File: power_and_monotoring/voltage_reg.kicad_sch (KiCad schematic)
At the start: 15 parts, among them IC1 ADP3335ARMZ-5-R7, IC2 ADP3335ARMZ-3.3-RL, J1 Microfit_01x02_Vertical, U10 P783-Q24-S3-S

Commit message: before design review
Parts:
- removed GLV_MASTER_IN1: GREEN, LTST-S270KGKT, UniSA_Motorsport_Diode:0605, symbol UniSA_Motorsport_Diode:LTST-S270KGKT
- added D5: GREEN, UniSA_Motorsport_Diode:0805, symbol UniSA_Motorsport_Diode:LED_0805
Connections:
- net GND: now also D5.1 (K)
- net at R39.2: now also D5.2 (A)
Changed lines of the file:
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@@
     (stroke (width 0) (type default))
   )
-  (wire (pts (xy 135.89 147.32) (xy 135.89 156.21))
+  (wire (pts (xy 135.89 139.7) (xy 135.89 156.21))
     (stroke (width 0) (type default))
   )
@@
         (path "/e288a49a-7ef7-4ddb-8751-b5872bff5868/00000000-0000-0000-0000-00005fc1883e"
           (reference "#PWR026") (unit 1)
+        )
+      )
+    )
+  )
+  (symbol (lib_id "UniSA_Motorsport_Diode:LED_0805") (at 135.89 135.89 90) (unit 1)
+    (in_bom yes) (on_board yes) (dnp no) (fields_autoplaced)
+    (property "Reference" "D5" (at 139.065 136.8552 90)
+      (effects (font (size 1.27 1.27)) (justify right))
+    )
+    (property "Value" "GREEN" (at 139.065 139.3952 90)
+      (effects (font (size 1.27 1.27)) (justify right))
+    )
+    (property "Footprint" "UniSA_Motorsport_Diode:0805" (at 135.89 135.89 0)
+      (effects (font (size 1.27 1.27)) hide)
+    )
+    (property "Datasheet" "https://au.mouser.com/datasheet/2/109/Dialight_CBI_data_599-0805_Apr2018-1370606.pdf" (at 135.89 135.89 0)
+      (effects (font (size 1.27 1.27)) hide)
+    )
+    (property "Color" "Red, Blue, Green, Orange, Yellow" (at 130.81 135.89 0)
+      (effects (font (size 1.27 1.27)) hide)
+    )
+    (pin "1")
+    (pin "2")
+    (instances
+      (project "power_and_monotoring"
+        (path "/09bdaed7-9abd-4a06-aca9-25dcfc39eec3/22f29577-e4ea-44ad-b176-4b72d277bfff"
+          (reference "D5") (unit 1)
+        )
+        (path "/09bdaed7-9abd-4a06-aca9-25dcfc39eec3/07532015-f4dd-4bfc-83f6-71cf6465f622"
+          (reference "D9") (unit 1)
+        )
+        (path "/09bdaed7-9abd-4a06-aca9-25dcfc39eec3/7e02ab45-3a69-40b9-bad8-957e9bf8bfd2"
+          (reference "D11") (unit 1)
         )
       )
@@
         )
       )
-    )
-  )
-  (symbol (lib_id "UniSA_Motorsport_Diode:LTST-S270KGKT") (at 135.89 139.7 90) (unit 1)
-    (in_bom yes) (on_board yes) (dnp no)
-    (property "Reference" "GLV_MASTER_IN1" (at 131.445 146.685 0)
-      (effects (font (size 1.27 1.27)))
-    )
-    (property "Value" "GREEN, LTST-S270KGKT" (at 129.54 149.225 0)
-      (effects (font (size 1.27 1.27)))
-    )
-    (property "Footprint" "UniSA_Motorsport_Diode:0605" (at 140.64 151.13 0)
-      (effects (font (size 1.27 1.27)) (justify left bottom) hide)
-    )
-    (property "Datasheet" "https://optoelectronics.liteon.com/upload/download/DS22-2000-226/LTST-S270KGKT.pdf" (at 140.97 182.88 0)
-      (effects (font (size 1.27 1.27)) (justify left bottom) hide)
-    )
-    (property "Height" "0.7" (at 529.54 127 0)
-      (effects (font (size 1.27 1.27)) (justify left bottom) hide)
-    )
-    (property "Mouser Part Number" "859-LTST-S270KGKT" (at 629.54 127 0)
-      (effects (font (size 1.27 1.27)) (justify left bottom) hide)
-    )
-    (property "Mouser Price/Stock" "https://www.mouser.co.uk/ProductDetail/Lite-On/LTST-S270KGKT?qs=oL5uk4n%2FG821%2FMiCU6RADg%3D%3D" (at 729.54 127 0)
-      (effects (font (size 1.27 1.27)) (justify left bottom) hide)
-    )
-    (property "Manufacturer_Name" "Lite-On" (at 829.54 127 0)
-      (effects (font (size 1.27 1.27)) (justify left bottom) hide)
-    )
-    (property "Manufacturer_Part_Number" "LTST-S270KGKT" (at 929.54 127 0)
-      (effects (font (size 1.27 1.27)) (justify left bottom) hide)
-    )
-    (pin "1")
-    (pin "2")
-    (instances
-      (project "power_and_monotoring"
-        (path "/09bdaed7-9abd-4a06-aca9-25dcfc39eec3/07532015-f4dd-4bfc-83f6-71cf6465f622"
-          (reference "GLV_MASTER_IN1") (unit 1)
-        )
-        (path "/09bdaed7-9abd-4a06-aca9-25dcfc39eec3/7e02ab45-3a69-40b9-bad8-957e9bf8bfd2"
-          (reference "LED11") (unit 1)
-        )
-      )

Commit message: Final
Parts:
- removed C16, C17: C, Capacitor_SMD:C_0805_2012Metric, symbol Device:C
- removed TP1: TestPoint, TestPoint:TestPoint_Pad_D2.0mm, symbol Connector:TestPoint
- removed U10: P783-Q24-S3-S, UniSA_Motorsport_Others:P783-Q24-S3-S, symbol UniSA_Motorsport_Regulator:P783-Q24-S3-S
- added 12V1: TestPoint, TestPoint:TestPoint_Pad_D2.0mm, symbol Connector:TestPoint
- added C6: 100uF, UniSA_Motorsport_Capacitor:EEEFK0J332AQ, symbol UniSA_Motorsport_Capacitor:EEE-FK1H101P
- added C8: EEV-FK1H391Q, UniSA_Motorsport_Capacitor:EEEFK0J332AQ, symbol UniSA_Motorsport_Capacitor:EEV-FK1H391Q
- added D27: NRVTS245ESFT1G, UniSA_Motorsport_Diode:SOD-123FL-2, symbol UniSA_Motorsport_Diode:NRVTS245ESFT1G
- added IC3: LM2576-12WU-TR, UniSA_Motorsport_SO:TO-263-5, symbol UniSA_Motorsport_Regulator:LM2576-12WU-TR
- added L1: 100uH, UniSA_Motorsport_Inductor:5050, symbol UniSA_Motorsport_Inductor:SRR1260-101M
- R23: renamed from R39; Resistance 68K -> 1K
- renumbered TP1 to 3V3, TP1 to 5V1, D5 to D11
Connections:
- net 12V is gone; now on net +12V: R23.1
- net +12V: now also 12V1.1, C8.1 (+), IC3.4 (FEEDBACK), L1.2
- net +24V: now also C6.1 (+), IC3.1 (VIN)
- net GND: now also C6.2 (-), C8.2 (-), D27.2 (A), IC3.3 (GROUND), IC3.5 (~{ON}/OFF), IC3.6 (GND)
- new net Reg_out: D27.1 (K), IC3.2 (OUTPUT), L1.1
- no-connect marks 6 -> 4
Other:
- moved on the sheet: D11, R23

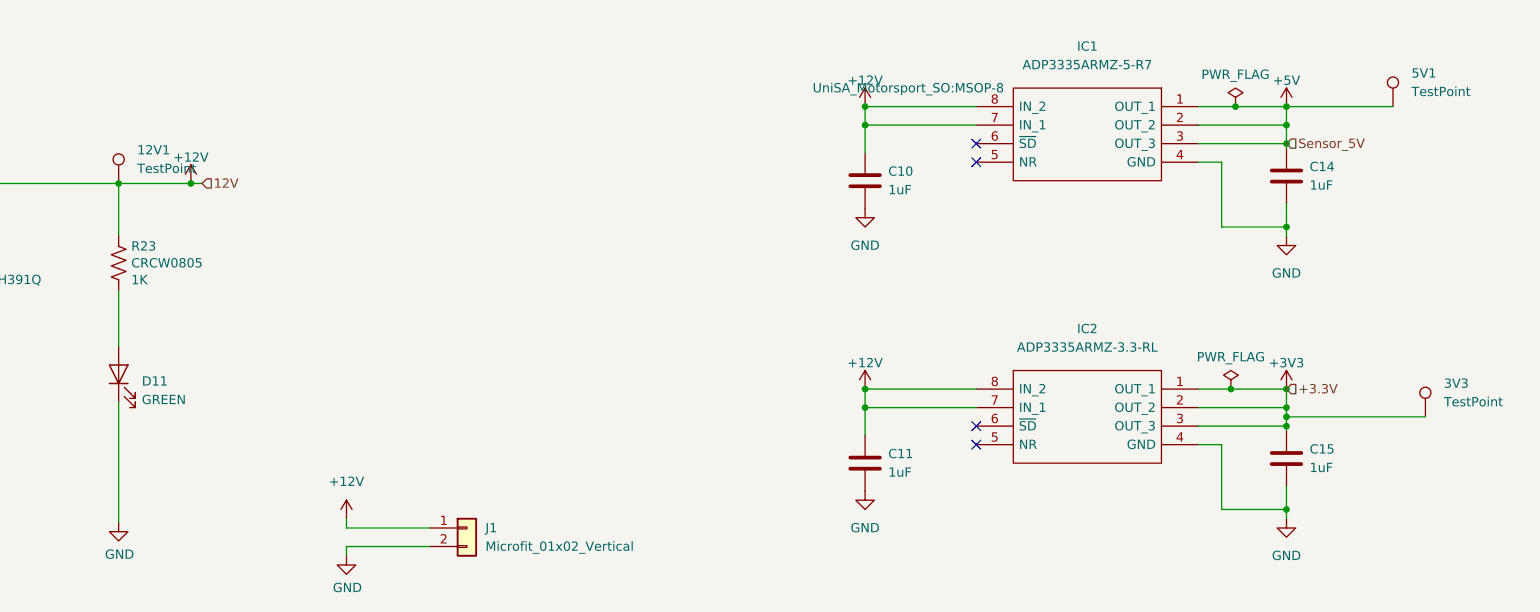
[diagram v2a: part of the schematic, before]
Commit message: Made it 4 layers
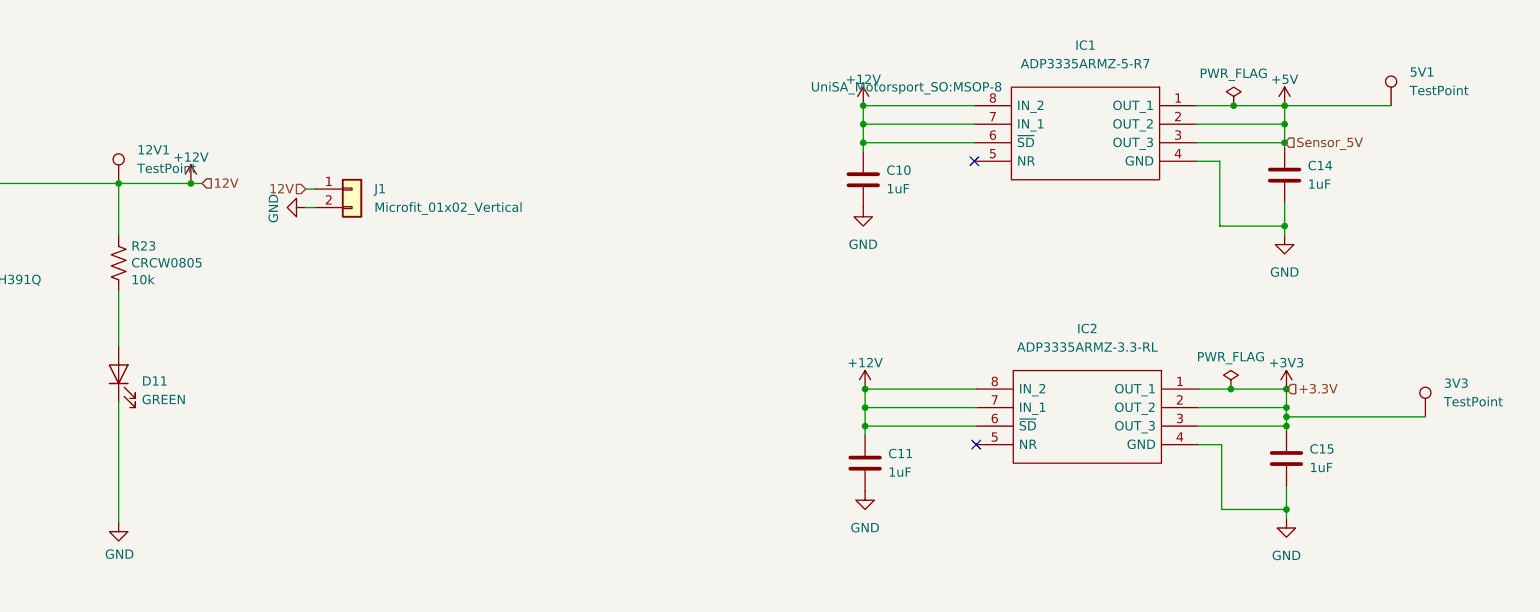
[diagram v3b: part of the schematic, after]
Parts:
- R23: Resistance 1K -> 10k
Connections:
- net +12V: now also IC1.6 (~{SD}), IC2.6 (~{SD})
- no-connect marks 4 -> 2
